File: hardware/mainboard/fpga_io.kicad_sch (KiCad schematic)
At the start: 24 parts, among them U1 LIFCL_40_CABGA400, X1 XO32

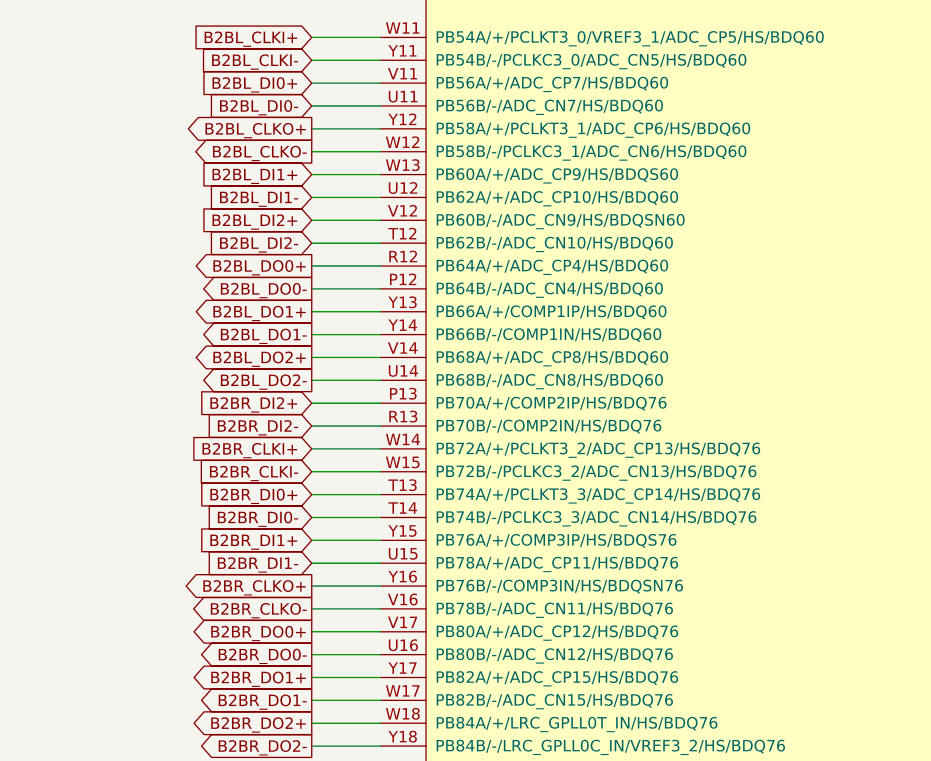
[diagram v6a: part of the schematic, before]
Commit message: Interboard pair routing
Signed-off-by: David Shah <dave@ds0.me>
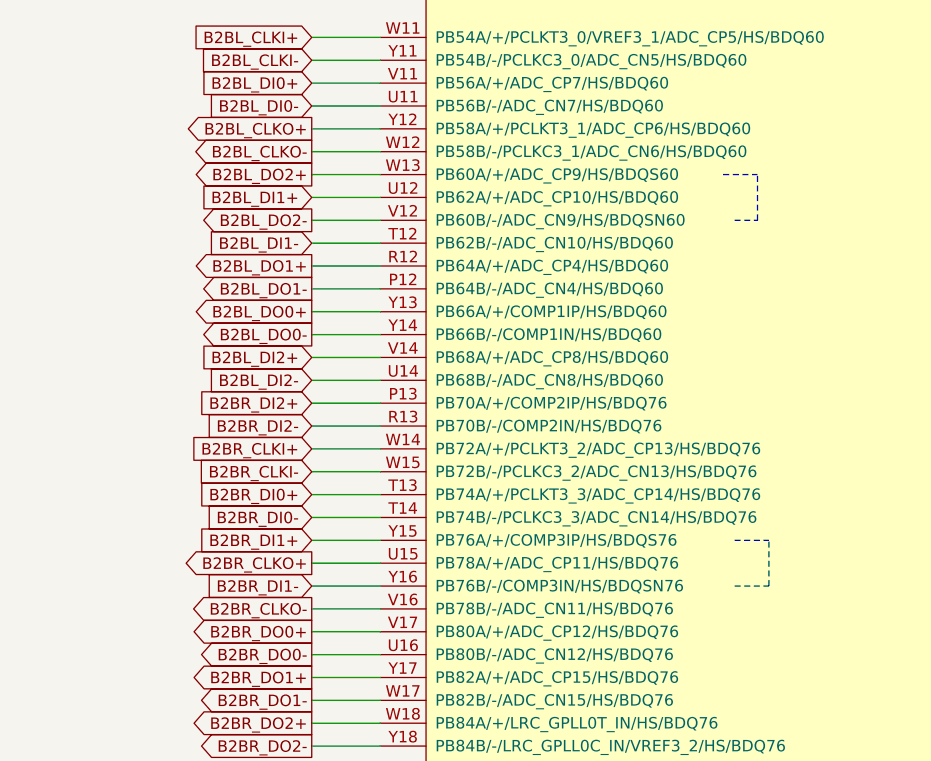
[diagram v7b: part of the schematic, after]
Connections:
- net B2BL_DI1+: now also U1.U12 (PB62A/+/ADC_CP10/HS/BDQ60); no longer U1.W13 (PB60A/+/ADC_CP9/HS/BDQS60)
- net B2BL_DI1-: now also U1.T12 (PB62B/-/ADC_CN10/HS/BDQ60); no longer U1.U12 (PB62A/+/ADC_CP10/HS/BDQ60)
- net B2BL_DI2+: now also U1.V14 (PB68A/+/ADC_CP8/HS/BDQ60); no longer U1.V12 (PB60B/-/ADC_CN9/HS/BDQSN60)
- net B2BL_DI2-: now also U1.U14 (PB68B/-/ADC_CN8/HS/BDQ60); no longer U1.T12 (PB62B/-/ADC_CN10/HS/BDQ60)
- net B2BL_DO0+: now also U1.Y13 (PB66A/+/COMP1IP/HS/BDQ60); no longer U1.R12 (PB64A/+/ADC_CP4/HS/BDQ60)
- net B2BL_DO0-: now also U1.Y14 (PB66B/-/COMP1IN/HS/BDQ60); no longer U1.P12 (PB64B/-/ADC_CN4/HS/BDQ60)
- net B2BL_DO1+: now also U1.R12 (PB64A/+/ADC_CP4/HS/BDQ60); no longer U1.Y13 (PB66A/+/COMP1IP/HS/BDQ60)
- net B2BL_DO1-: now also U1.P12 (PB64B/-/ADC_CN4/HS/BDQ60); no longer U1.Y14 (PB66B/-/COMP1IN/HS/BDQ60)
- net B2BL_DO2+: now also U1.W13 (PB60A/+/ADC_CP9/HS/BDQS60); no longer U1.V14 (PB68A/+/ADC_CP8/HS/BDQ60)
- net B2BL_DO2-: now also U1.V12 (PB60B/-/ADC_CN9/HS/BDQSN60); no longer U1.U14 (PB68B/-/ADC_CN8/HS/BDQ60)
- net B2BR_CLKO+: now also U1.U15 (PB78A/+/ADC_CP11/HS/BDQ76); no longer U1.Y16 (PB76B/-/COMP3IN/HS/BDQSN76)
- net B2BR_DI1-: now also U1.Y16 (PB76B/-/COMP3IN/HS/BDQSN76); no longer U1.U15 (PB78A/+/ADC_CP11/HS/BDQ76)
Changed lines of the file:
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@@
     (stroke (width 0) (type solid) (color 0 0 0 0))
+  )
+  (polyline (pts (xy 210.82 60.96) (xy 214.63 60.96))
+    (stroke (width 0) (type dash) (color 0 0 0 0))
+  )
+  (polyline (pts (xy 212.09 66.04) (xy 214.63 66.04))
+    (stroke (width 0) (type dash) (color 0 0 0 0))
+  )
+  (polyline (pts (xy 212.09 101.6) (xy 215.9 101.6))
+    (stroke (width 0) (type dash) (color 0 0 0 0))
+  )
+  (polyline (pts (xy 212.09 106.68) (xy 215.9 106.68))
+    (stroke (width 0) (type dash) (color 0 0 0 0))
+  )
+  (polyline (pts (xy 214.63 66.04) (xy 214.63 60.96))
+    (stroke (width 0) (type dash) (color 0 0 0 0))
+  )
+  (polyline (pts (xy 215.9 106.68) (xy 215.9 101.6))
+    (stroke (width 0) (type dash) (color 0 0 0 0))
   )
   (label "CLK48" (at 50.8 125.73 0)
@@
     )
   )
-  (global_label "B2BL_DI1+" (shape input) (at 165.1 60.96 180)
-    (effects (font (size 1.27 1.27)) (justify right))
-    (property "Intersheet References" "${INTERSHEET_REFS}" (id 0) (at 150.761 60.8806 0)
-      (effects (font (size 1.27 1.27)) (justify right) hide)
-    )
-  )
-  (global_label "B2BL_DI1-" (shape input) (at 165.1 63.5 180)
+  (global_label "B2BL_DO2+" (shape output) (at 165.1 60.96 180)
+    (effects (font (size 1.27 1.27)) (justify right))
+    (property "Intersheet References" "${INTERSHEET_REFS}" (id 0) (at 150.0353 60.8806 0)
+      (effects (font (size 1.27 1.27)) (justify right) hide)
+    )
+  )
+  (global_label "B2BL_DI1+" (shape input) (at 165.1 63.5 180)
     (effects (font (size 1.27 1.27)) (justify right))
     (property "Intersheet References" "${INTERSHEET_REFS}" (id 0) (at 150.761 63.4206 0)
@@
     )
   )
-  (global_label "B2BL_DI2+" (shape input) (at 165.1 66.04 180)
-    (effects (font (size 1.27 1.27)) (justify right))
-    (property "Intersheet References" "${INTERSHEET_REFS}" (id 0) (at 150.761 65.9606 0)
-      (effects (font (size 1.27 1.27)) (justify right) hide)
-    )
-  )
-  (global_label "B2BL_DI2-" (shape input) (at 165.1 68.58 180)
+  (global_label "B2BL_DO2-" (shape output) (at 165.1 66.04 180)
+    (effects (font (size 1.27 1.27)) (justify right))
+    (property "Intersheet References" "${INTERSHEET_REFS}" (id 0) (at 150.0353 65.9606 0)
+      (effects (font (size 1.27 1.27)) (justify right) hide)
+    )
+  )
+  (global_label "B2BL_DI1-" (shape input) (at 165.1 68.58 180)
     (effects (font (size 1.27 1.27)) (justify right))
     (property "Intersheet References" "${INTERSHEET_REFS}" (id 0) (at 150.761 68.5006 0)
@@
     )
   )
-  (global_label "B2BL_DO0+" (shape output) (at 165.1 71.12 180)
+  (global_label "B2BL_DO1+" (shape output) (at 165.1 71.12 180)
     (effects (font (size 1.27 1.27)) (justify right))
     (property "Intersheet References" "${INTERSHEET_REFS}" (id 0) (at 150.0353 71.0406 0)
@@
     )
   )
-  (global_label "B2BL_DO0-" (shape output) (at 165.1 73.66 180)
+  (global_label "B2BL_DO1-" (shape output) (at 165.1 73.66 180)
     (effects (font (size 1.27 1.27)) (justify right))
     (property "Intersheet References" "${INTERSHEET_REFS}" (id 0) (at 150.0353 73.5806 0)
@@
     )
   )
-  (global_label "B2BL_DO1+" (shape output) (at 165.1 76.2 180)
+  (global_label "B2BL_DO0+" (shape output) (at 165.1 76.2 180)
     (effects (font (size 1.27 1.27)) (justify right))
     (property "Intersheet References" "${INTERSHEET_REFS}" (id 0) (at 150.0353 76.1206 0)
@@
     )
   )
-  (global_label "B2BL_DO1-" (shape output) (at 165.1 78.74 180)
+  (global_label "B2BL_DO0-" (shape output) (at 165.1 78.74 180)
     (effects (font (size 1.27 1.27)) (justify right))
     (property "Intersheet References" "${INTERSHEET_REFS}" (id 0) (at 150.0353 78.6606 0)
@@
     )
   )
-  (global_label "B2BL_DO2+" (shape output) (at 165.1 81.28 180)
-    (effects (font (size 1.27 1.27)) (justify right))
-    (property "Intersheet References" "${INTERSHEET_REFS}" (id 0) (at 150.0353 81.2006 0)
-      (effects (font (size 1.27 1.27)) (justify right) hide)
-    )
-  )
-  (global_label "B2BL_DO2-" (shape output) (at 165.1 83.82 180)
-    (effects (font (size 1.27 1.27)) (justify right))
-    (property "Intersheet References" "${INTERSHEET_REFS}" (id 0) (at 150.0353 83.7406 0)
+  (global_label "B2BL_DI2+" (shape input) (at 165.1 81.28 180)
+    (effects (font (size 1.27 1.27)) (justify right))
+    (property "Intersheet References" "${INTERSHEET_REFS}" (id 0) (at 150.761 81.2006 0)
+      (effects (font (size 1.27 1.27)) (justify right) hide)
+    )
+  )
+  (global_label "B2BL_DI2-" (shape input) (at 165.1 83.82 180)
+    (effects (font (size 1.27 1.27)) (justify right))
+    (property "Intersheet References" "${INTERSHEET_REFS}" (id 0) (at 150.761 83.7406 0)
       (effects (font (size 1.27 1.27)) (justify right) hide)
     )
@@
     )
   )
-  (global_label "B2BR_DI1-" (shape input) (at 165.1 104.14 180)
-    (effects (font (size 1.27 1.27)) (justify right))
-    (property "Intersheet References" "${INTERSHEET_REFS}" (id 0) (at 150.5191 104.0606 0)
-      (effects (font (size 1.27 1.27)) (justify right) hide)
-    )
-  )
-  (global_label "B2BR_CLKO+" (shape output) (at 165.1 106.68 180)
-    (effects (font (size 1.27 1.27)) (justify right))
-    (property "Intersheet References" "${INTERSHEET_REFS}" (id 0) (at 148.7048 106.6006 0)
-      (effects (font (size 1.27 1.27)) (justify right) hide)
-    )
+  (global_label "B2BR_CLKO+" (shape output) (at 165.1 104.14 180)
+    (effects (font (size 1.27 1.27)) (justify right))
+    (property "Intersheet References" "${INTERSHEET_REFS}" (id 0) (at 148.7048 104.0606 0)
+      (effects (font (size 1.27 1.27)) (justify right) hide)
+    )
+  )
+  (global_label "B2BR_DI1-" (shape input) (at 165.1 106.68 180)
+    (effects (font (size 1.27 1.27)) (justify right))
+    (property "Intersheet References" "${INTERSHEET_REFS}" (id 0) (at 150.5191 106.6006 0)
+      (effects (font (size 1.27 1.27)) (justify right) hide)
+    )

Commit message: More misc routing
Signed-off-by: David Shah <dave@ds0.me>
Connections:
- net BTN_1 is gone; now on net EAR_0: U1.R1 (PL47A/+)
- net B2BL_MISC0: no longer U1.E9 (PL10B/-)
- net B2BL_MISC1: no longer U1.E7 (PL11A/+)
- net B2BL_MISC2: no longer U1.E8 (PL11B/-)
- net B2BR_MISC0: now also U1.R5 (PB10A/+/PCLKT5_2/ADC_CP2/COMP3P/HS); no longer U1.E4 (PL13A/+), U1.Y2 (PB8A/+/PCLKT5_1/LLC_GPLL0T_IN/ADC_CP3/HS)
- net B2BR_MISC1: no longer U1.E3 (PL13B/-)
- net B2BR_MISC2: now also U1.Y2 (PB8A/+/PCLKT5_1/LLC_GPLL0T_IN/ADC_CP3/HS); no longer U1.E2 (PL15A/+), U1.R5 (PB10A/+/PCLKT5_2/ADC_CP2/COMP3P/HS)
- net DISP_~RESET: now also U1.F1 (PL15B/-); no longer U1.D3 (PL8B/-)
- net EAR_0: no longer U1.N6 (PL42A/+)
- net EAR_1: now also U1.R2 (PL47B/-); no longer U1.N7 (PL42B/-)
- net IMU_CLK: now also U1.J1 (PL17B/-); no longer U1.D6 (PL6A/+)
- net IMU_DI: now also U1.E2 (PL15A/+); no longer U1.D8 (PL4B/-)
- net IMU_DO: now also U1.J2 (PL17A/+/PCLKT7_2); no longer U1.D7 (PL4A/+)
- net IMU_FSYNC: now also U1.K1 (PL19B/-); no longer U1.D4 (PL8A/+)
- net IMU_~CS: now also U1.K2 (PL19A/+/PCLKT7_1); no longer U1.D5 (PL6B/-)
- net LED_1: now also U1.L2 (PL27B/-); no longer U1.K5 (PL24A/+)
- net LED_6: now also U1.K5 (PL24A/+); no longer U1.L2 (PL27B/-)
- net PMOD1_1: now also U1.G19 (PR13B/-); no longer U1.L14 (PR17B/-)
- net PMOD1_10: now also U1.G14 (PR15A/+); no longer U1.F16 (PR8A/+)
- net PMOD1_2: now also U1.F18 (PR10A/+); no longer U1.G14 (PR15A/+)
- net PMOD1_4: now also U1.L14 (PR17B/-); no longer U1.G19 (PR13B/-)
- net PMOD1_9: now also U1.F16 (PR8A/+); no longer U1.F18 (PR10A/+)
- net BTN_0 renamed BTN0
- new net BTN1: U1.N6 (PL42A/+)
